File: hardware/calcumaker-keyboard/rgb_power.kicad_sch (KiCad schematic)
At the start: 9 parts, among them Q1 AO3401A, Q2 2N7002, U2 74LVC1G125

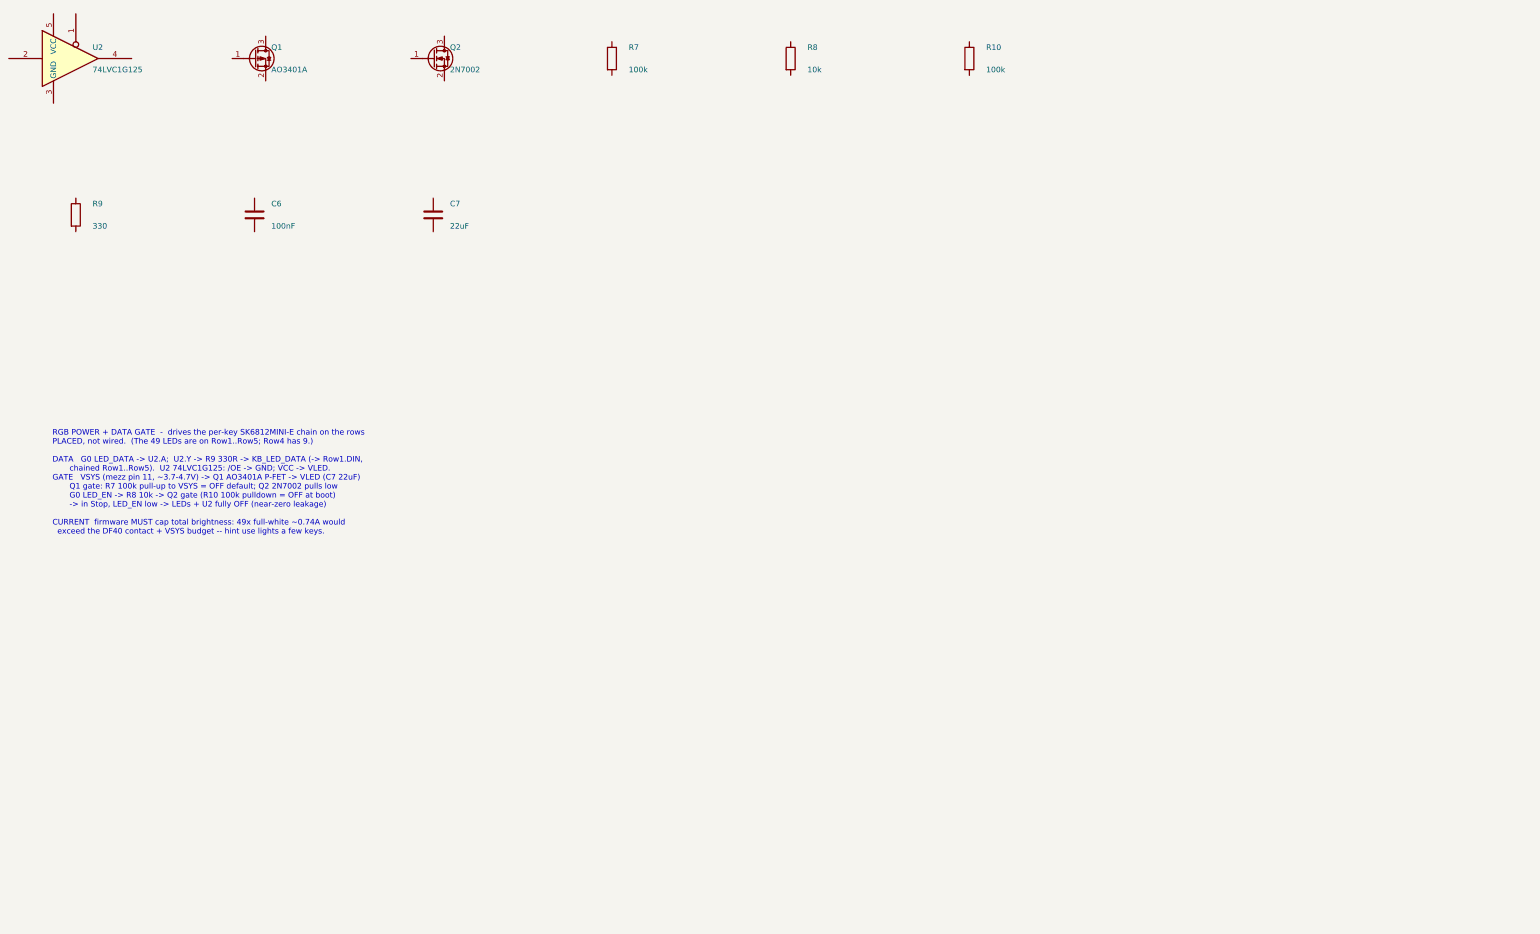
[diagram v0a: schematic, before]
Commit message: Wire mainboard and keypad schematics and verify expanded nets
Connect hierarchical interfaces, power/control circuits, debug links, matrix and RGB chains. Correct MCU package pins, diode polarity and power configuration; add bypass components and repeatable KiCad netlist/ERC checks. Document pin maps and remaining physical validation.
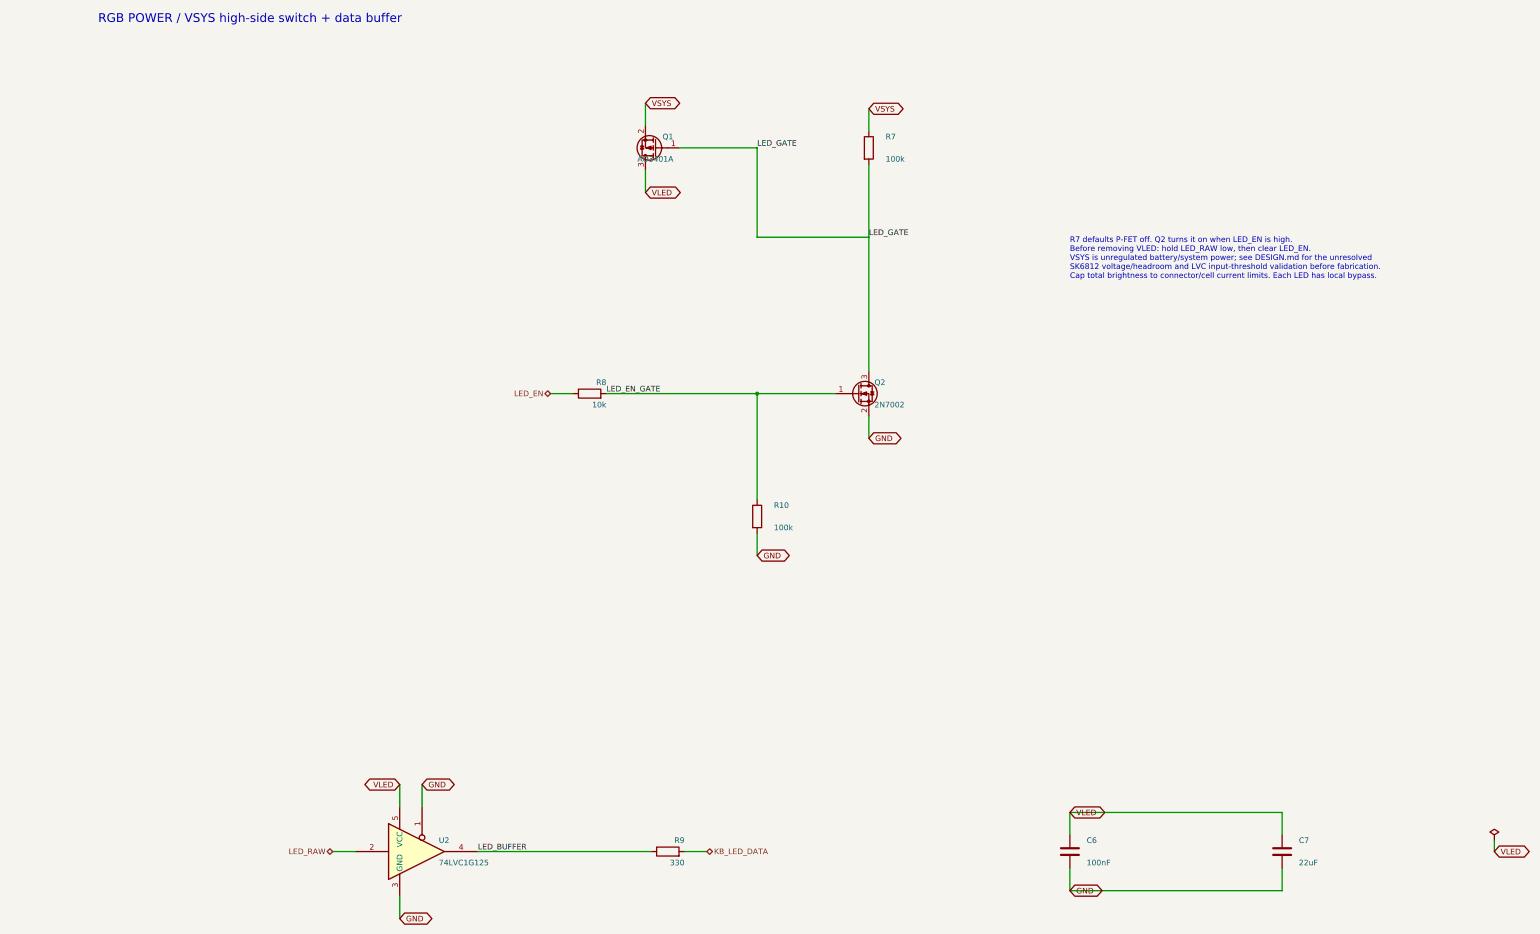
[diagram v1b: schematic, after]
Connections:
- net LED_BUFFER: now reaches R9.1
- net LED_BUFFER: now also U2.4
- net KB_LED_DATA: now reaches R9.2
- net LED_GATE: now reaches Q1.1 (G)
- net LED_GATE: now also Q2.3 (D), R7.2
- net VSYS: now reaches Q1.2 (S)
- net VSYS: now also R7.1
- net VLED: now reaches Q1.3 (D)
- net VLED: now also C6.1, C7.1, U2.5 (VCC)
- net GND: now reaches C6.2
- net GND: now also C7.2, Q2.2 (S), R10.2, U2.1, U2.3 (GND)
- net LED_EN_GATE: now reaches Q2.1 (G)
- net LED_EN_GATE: now also R10.1, R8.2
- net LED_EN: now reaches R8.1
- net LED_RAW: now reaches U2.2
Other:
- note added: "R7 defaults P-FET off. Q2 turns it on when LED_EN is high. Before removing VLED: hold LED_RAW low, then clear LED_EN. VSYS is unregulated battery/system power; see DESIGN.md for the unresolved SK6812 voltage/headroom and LVC input-threshold validation before fabrication. Cap total brightness to connector/cell current limits. Each LED has local bypass."
- note added: "RGB POWER / VSYS high-side switch + data buffer"
- note removed: "RGB POWER + DATA GATE - drives the per-key SK6812MINI-E chain on the rows PLACED, not wired. (The 49 LEDs are on Row1..Row5; Row4 has 9.) DATA G0 LED_DATA -> U2.A; U2.Y -> R9 330R -> KB_LED_DATA (-> Row1.DIN, chained Row1..Row5). U2 74LVC1G125: /OE -> GND; VCC -> VLED. GATE VSYS (mezz pin 11, ~3.7-4.7V) -> Q1 AO3401A P-FET -> VLED (C7 22uF) Q1 gate: R7 100k pull-up to VSYS = OFF default; Q2 2N700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"
- title: Calcumaker 16 — Keyboard — RGB power + data gate (level shift + load switch) -> Calcumaker 16 / keyboard / rgb power
- moved on the sheet: C6, C7, Q1, Q2, R10, R7, R8, R9, U2
